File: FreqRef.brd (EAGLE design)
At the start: 50.8 x 43.2 mm, 33 parts, among them J1 ISP Connector, J2 BNC_RIGHT-ANGLE, SW1 PWR, U1 ATMEGA328, U2 MIC5205, U3 SN74LV164APW

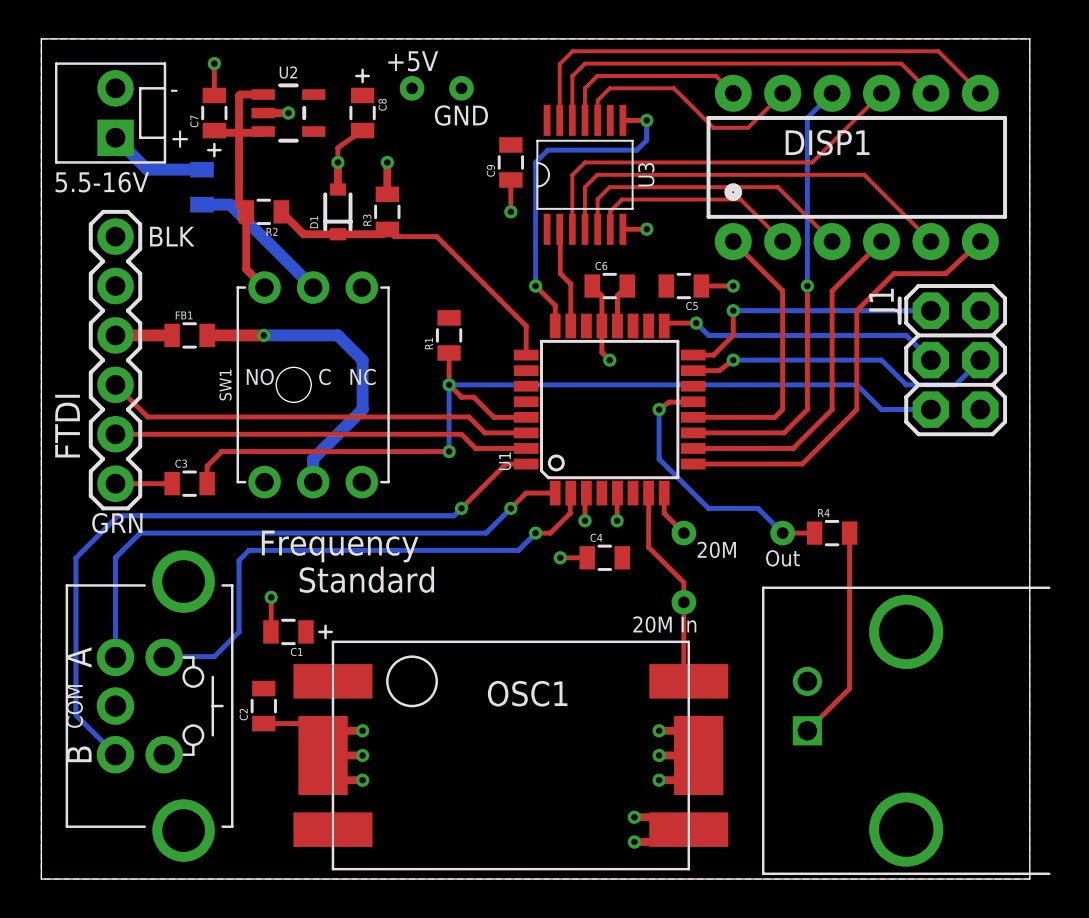
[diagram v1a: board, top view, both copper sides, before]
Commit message: More docs. Rev-B layout. Debugged sketch.
Continue documentation. Added two oscillator options to PCB schematic
and layout.  Debugged sketch  on Redboard.
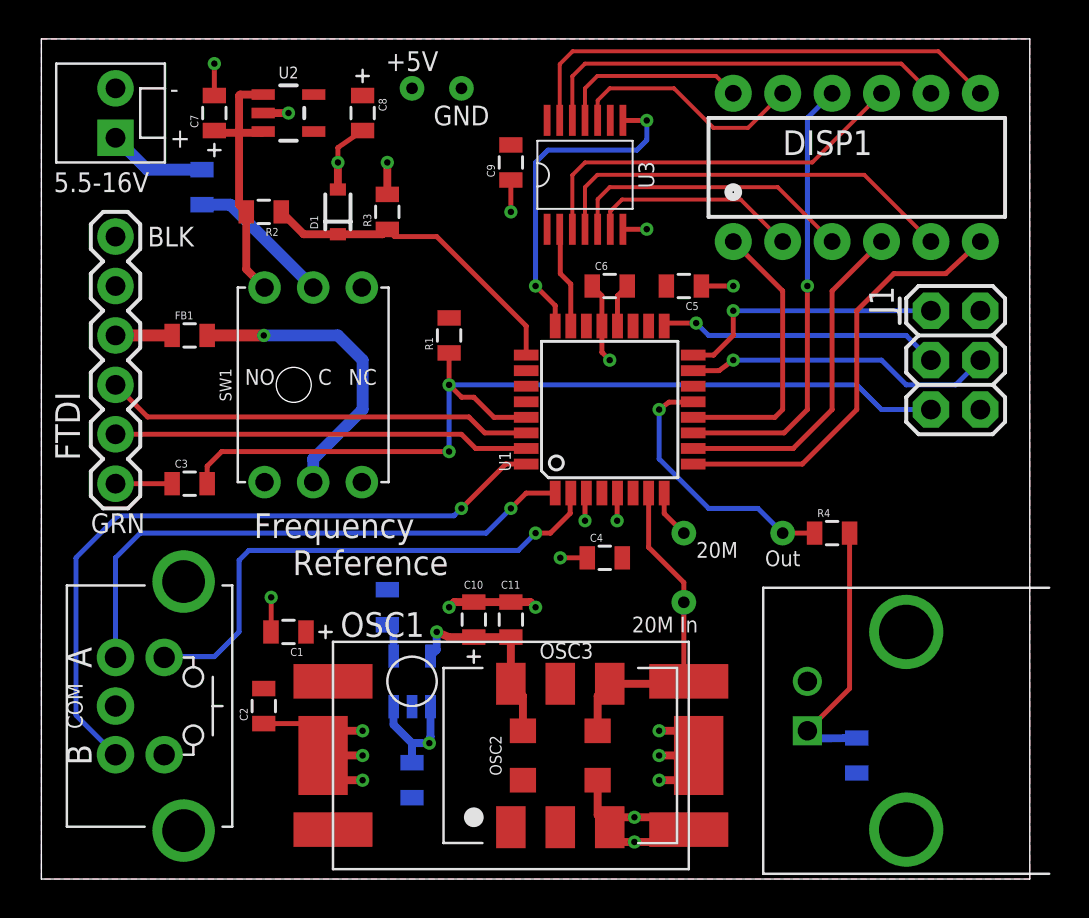
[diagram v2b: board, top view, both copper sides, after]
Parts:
- added C10, C13: 10uF, ChipsParts:0805-POL
- added C11: 10nF, SparkFun-Capacitors:0805
- added C12: 470pF, SparkFun-Capacitors:0805
- added C14: 50pF, SparkFun-Capacitors:0805
- added OSC2: (no value), playground:TCXO-3.2X5
- added OSC3: (no value), playground:TCXO-9X14
- added U5: MIC5219 3.3V, SparkFun-PowerIC:SOT23-5
- U1: value ATMEGA328 -> ATMEGA328P
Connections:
- net N$31 renamed VIN
- removed net N$5: OSC1.OUT, TP3.P$1, U1.7
- new net N$14: C10.1, C11.1, OSC2.8, OSC3.6, U5.5
- new net N$15: C12.1, U5.4
- new net OSCIN: OSC1.OUT, OSC2.5, OSC3.4, TP3.P$1, U1.7
- net GND: now also C10.2, C11.2, C12.2, C13.2, C14.2, OSC2.4, OSC3.3, U5.2
- net N$11: now also C14.1
- net VCC: now also C13.1, U5.1, U5.3
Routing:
- net OSCIN: track 0.00 -> 17.4 mm
- net GND: track 42.7 -> 53.7 mm, vias 20 -> 22
- net N$5: track 10.5 -> 0.00 mm
- net N$14: track 0.00 -> 10.3 mm, vias 0 -> 1
- net VCC: track 0.00 -> 6.04 mm, vias 0 -> 1
- net N$11: track 11.1 -> 13.7 mm
- net N$15: track 0.00 -> 1.74 mm
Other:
- board text added: "Frequency Reference"
- board text added: "http://github.com/uchip/FrequencyReference"
- board text removed: "Frequency Standard"
- board text removed: "http://github.com/uchip/FrequencyStandard"
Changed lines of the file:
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@@
 <text x="30.353" y="13.081" size="0.8128" layer="21" font="vector" ratio="15" align="center-left">20M In</text>
 <text x="33.655" y="16.51" size="0.8128" layer="21" font="vector" ratio="15">20M</text>
-<text x="11.176" y="14.732" size="1.27" layer="21" font="vector" ratio="15">Frequency
-    Standard</text>
-<text x="46.99" y="5.08" size="1.27" layer="22" font="vector" ratio="15" rot="MR45">http://github.com/uchip/FrequencyStandard</text>
+<text x="10.922" y="15.621" size="1.27" layer="21" font="vector" ratio="15">Frequency
+    Reference</text>
+<text x="48.26" y="3.81" size="1.27" layer="22" font="vector" ratio="15" rot="MR45">http://github.com/uchip/FrequencyReference</text>
 </plain>
 <attributes>
@@
 <elements>
 <element name="OSC1" library="playground" package="TCXO" value="" x="24.13" y="6.35" smashed="yes">
-<attribute name="NAME" x="22.86" y="8.89" size="1.27" layer="25" font="vector" ratio="15"/>
+<attribute name="NAME" x="15.367" y="12.446" size="1.27" layer="25" font="vector" ratio="15"/>
 <attribute name="VALUE" x="24.13" y="-1.27" size="1.27" layer="27" font="vector" ratio="15" align="bottom-center"/>
 </element>
@@
 <attribute name="VALUE" x="12.5095" y="40.3225" size="0.4064" layer="27" rot="R270"/>
 </element>
-<element name="U1" library="SparkFun" package="TQFP32-08" value="ATMEGA328" x="29.21" y="24.13" smashed="yes" rot="R90">
+<element name="U1" library="SparkFun" package="TQFP32-08" value="ATMEGA328P" x="29.21" y="24.13" smashed="yes" rot="R90">
 <attribute name="NAME" x="24.13" y="20.955" size="0.6096" layer="25" ratio="15" rot="R90"/>
 <attribute name="VALUE" x="35.56" y="21.59" size="0.4064" layer="27" rot="R90"/>
@@
 </element>
 <element name="FRAME1" library="NewFrame" package="FR-LTR-ON-PCB" value="FRAME_LTR_CU_MARK" x="49.53" y="17.78">
-<attribute name="CNAME" value="Frequency Standard" x="49.53" y="17.78" size="1.778" layer="27" display="off"/>
-<attribute name="CREVISION" value="Rev B" x="49.53" y="17.78" size="1.778" layer="27" display="off"/>
+<attribute name="CNAME" value="Frequency Reference" x="49.53" y="17.78" size="1.778" layer="27" display="off"/>
+<attribute name="CREVISION" value="Rev-B" x="49.53" y="17.78" size="1.778" layer="27" display="off"/>
 <attribute name="DATECODE" value="2015" x="49.53" y="17.78" size="1.778" layer="27" display="off"/>
 <attribute name="DESIGNER" value="C.Schnarel" x="49.53" y="17.78" size="1.778" layer="27" display="off"/>
 </element>
 <element name="TP4" library="ChipsParts" package="BBD-VIA" value="TEST_POINT" x="33.02" y="17.78"/>
+<element name="OSC2" library="playground" package="TCXO-3.2X5" value="" x="26.67" y="6.35" smashed="yes" rot="R270">
+<attribute name="NAME" x="23.654" y="6.35" size="0.6096" layer="25" font="vector" ratio="15" rot="R90" align="bottom-center"/>
+<attribute name="VALUE" x="26.67" y="4.35" size="0.6096" layer="25" font="vector" ratio="15" align="top-center"/>
+</element>
+<element name="OSC3" library="playground" package="TCXO-9X14" value="" x="26.67" y="6.35" smashed="yes" rot="R270">
+<attribute name="NAME" x="25.599" y="11.326" size="0.8128" layer="25" font="vector" ratio="15"/>
+<attribute name="VALUE" x="20.17" y="6.35" size="0.8128" layer="27" font="vector" ratio="15" rot="R270" align="top-center"/>
+</element>
+<element name="C10" library="ChipsParts" package="0805-POL" value="10uF" x="22.225" y="13.335" smashed="yes" rot="R90">
+<attribute name="NAME" x="21.717" y="14.9225" size="0.4064" layer="25" ratio="15"/>
+<attribute name="VALUE" x="23.622" y="12.319" size="0.4064" layer="27" rot="R90"/>
+</element>
+<element name="C11" library="SparkFun-Capacitors" package="0805" value="10nF" x="24.13" y="13.335" smashed="yes" rot="R90">
+<attribute name="NAME" x="23.622" y="14.9225" size="0.4064" layer="25" ratio="15"/>
+<attribute name="VALUE" x="25.527" y="12.319" size="0.4064" layer="27" rot="R90"/>
+</element>
+<element name="C12" library="SparkFun-Capacitors" package="0805" value="470pF" x="17.78" y="13.97" rot="MR90"/>
+<element name="C13" library="ChipsParts" package="0805-POL" value="10uF" x="19.05" y="5.08" rot="MR270"/>
+<element name="U5" library="SparkFun-PowerIC" package="SOT23-5" value="MIC5219 3.3V" x="19.05" y="10.16" rot="MR0">
+<attribute name="PROD_ID" value="VREG-09872" x="19.05" y="10.16" size="1.778" layer="28" rot="MR0" display="off"/>
+</element>
+<element name="C14" library="SparkFun-Capacitors" package="0805" value="50pF" x="41.91" y="6.35" smashed="yes" rot="MR270">
+<attribute name="NAME" x="41.0845" y="7.112" size="0.4064" layer="26" ratio="15" rot="MR270"/>
+<attribute name="VALUE" x="43.307" y="7.366" size="0.4064" layer="28" rot="MR270"/>
+</element>
 </elements>
 <signals>
@@
 <wire x1="31.75" y1="2.54" x2="31.75" y2="3.175" width="0.4064" layer="1"/>
 <wire x1="31.75" y1="2.54" x2="33.274" y2="2.54" width="0.4064" layer="1"/>
+<contactref element="C10" pad="2"/>
+<contactref element="OSC3" pad="3"/>
+<contactref element="OSC2" pad="4"/>
+<contactref element="C11" pad="2"/>
+<via x="25.4" y="13.97" extent="1-16" drill="0.3302"/>
+<via x="20.955" y="13.97" extent="1-16" drill="0.3302"/>
+<wire x1="24.13" y1="14.235" x2="25.135" y2="14.235" width="0.4064" layer="1"/>
+<wire x1="25.135" y1="14.235" x2="25.4" y2="13.97" width="0.4064" layer="1"/>
+<wire x1="24.13" y1="14.235" x2="22.225" y2="14.235" width="0.4064" layer="1"/>
+<wire x1="22.225" y1="14.235" x2="21.22" y2="14.235" width="0.4064" layer="1"/>
+<wire x1="21.22" y1="14.235" x2="20.955" y2="13.97" width="0.4064" layer="1"/>
+<wire x1="28.59" y1="5.08" x2="28.59" y2="3.285" width="0.4064" layer="1"/>
+<wire x1="28.59" y1="3.285" x2="29.21" y2="2.665" width="0.4064" layer="1"/>
+<contactref element="C13" pad="2"/>
+<contactref element="C12" pad="2"/>
+<contactref element="U5" pad="2"/>
+<contactref element="C14" pad="2"/>
+<wire x1="30.48" y1="1.905" x2="29.21" y2="1.905" width="0.4064" layer="1"/>
+<wire x1="29.21" y1="1.905" x2="29.21" y2="2.54" width="0.4064" layer="1"/>
+<wire x1="30.48" y1="3.175" x2="29.21" y2="3.175" width="0.4064" layer="1"/>
+<wire x1="29.21" y1="3.175" x2="29.21" y2="2.665" width="0.4064" layer="1"/>
 <wire x1="33.02" y1="6.35" x2="33.782" y2="6.35" width="0" layer="19" extent="1-1"/>
 </signal>
@@
 <contactref element="U3" pad="9"/>
 <contactref element="U3" pad="1"/>
+<contactref element="U5" pad="3"/>
+<contactref element="C13" pad="1"/>
+<contactref element="U5" pad="1"/>
+<wire x1="20" y1="8.8599" x2="20" y2="7.305" width="0.4064" layer="16"/>
+<wire x1="20" y1="7.305" x2="19.939" y2="6.985" width="0.4064" layer="16"/>
+<via x="19.939" y="6.985" extent="1-16" drill="0.3302"/>
+<wire x1="19.05" y1="6.985" x2="18.1" y2="7.935" width="0.4064" layer="16"/>
+<wire x1="18.1" y1="7.935" x2="18.1" y2="8.8599" width="0.4064" layer="16"/>
+<wire x1="19.05" y1="6.985" x2="19.939" y2="6.985" width="0.4064" layer="16"/>
+<wire x1="19.05" y1="5.98" x2="19.05" y2="6.985" width="0.4064" layer="16"/>
 </signal>
 <signal name="RAW" class="1">
@@
 <wire x1="38.1" y1="17.78" x2="39.74" y2="17.78" width="0.254" layer="1"/>
 </signal>
-<signal name="N$5">
+<signal name="OSCIN">
 <contactref element="U1" pad="7"/>
 <contactref element="OSC1" pad="OUT"/>
@@
 <wire x1="33.02" y1="10.414" x2="33.274" y2="10.16" width="0.254" layer="1"/>
 <contactref element="TP3" pad="P$1"/>
+<contactref element="OSC2" pad="5"/>
+<contactref element="OSC3" pad="4"/>
+<wire x1="29.21" y1="10.035" x2="33.274" y2="10.035" width="0.4064" layer="1"/>
+<wire x1="33.274" y1="10.035" x2="33.274" y2="10.16" width="0.4064" layer="1"/>
+<wire x1="28.59" y1="7.62" x2="28.59" y2="9.415" width="0.4064" layer="1"/>
+<wire x1="28.59" y1="9.415" x2="29.21" y2="10.035" width="0.4064" layer="1"/>
 <wire x1="33.02" y1="15.24" x2="33.02" y2="14.224" width="0" layer="19" extent="1-1"/>
 </signal>
@@
 <wire x1="3.81" y1="27.94" x2="6.72" y2="27.94" width="0.6096" layer="1"/>
 </signal>
-<signal name="N$31">
+<signal name="VIN">
 <contactref element="SW1" pad="2C"/>
 <wire x1="9.71" y1="34.66" x2="13.97" y2="30.4" width="0.6096" layer="16"/>
@@
 <wire x1="39.37" y1="7.62" x2="41.54" y2="9.79" width="0.254" layer="1"/>
 <wire x1="41.54" y1="9.79" x2="41.54" y2="17.78" width="0.254" layer="1"/>
+<contactref element="C14" pad="1"/>
+<wire x1="41.91" y1="7.25" x2="39.867" y2="7.228" width="0.4064" layer="16"/>
+<wire x1="39.867" y1="7.228" x2="39.37" y2="7.62" width="0.4064" layer="16"/>
 </signal>
 <signal name="N$13">
@@
 <wire x1="5.45" y1="36.46" x2="8.255" y2="36.46" width="0.6096" layer="16"/>
 </signal>
+<signal name="N$14">
+<contactref element="OSC3" pad="6"/>
+<contactref element="C10" pad="1"/>
+<contactref element="C11" pad="1"/>
+<contactref element="OSC2" pad="8"/>
+<wire x1="24.13" y1="12.435" x2="24.13" y2="10.035" width="0.4064" layer="1"/>
+<wire x1="24.75" y1="7.62" x2="24.75" y2="9.415" width="0.4064" layer="1"/>
+<wire x1="24.75" y1="9.415" x2="24.13" y2="10.035" width="0.4064" layer="1"/>
+<wire x1="20.944" y1="12.435" x2="20.32" y2="12.7" width="0.4064" layer="1"/>
+<via x="20.32" y="12.7" extent="1-16" drill="0.3302"/>
+<contactref element="U5" pad="5"/>
+<wire x1="20.32" y1="12.7" x2="20.32" y2="11.7801" width="0.4064" layer="16"/>
+<wire x1="20.32" y1="11.7801" x2="20" y2="11.4601" width="0.4064" layer="16"/>
+<wire x1="20.944" y1="12.435" x2="22.225" y2="12.435" width="0.4064" layer="1"/>
+<wire x1="22.225" y1="12.435" x2="24.13" y2="12.435" width="0.4064" layer="1"/>
+</signal>
+<signal name="N$15">
+<contactref element="C12" pad="1"/>
+<contactref element="U5" pad="4"/>
+<wire x1="18.1" y1="11.4601" x2="18.1" y2="12.75" width="0.4064" layer="16"/>
+<wire x1="18.1" y1="12.75" x2="17.78" y2="13.07" width="0.4064" layer="16"/>
+</signal>
 </signals>

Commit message: Software debug.  Schematic values. Added photos.
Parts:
- R2: value 15k -> 10k
- R3: value 5k -> 3.3k
- moved C3 12.8 mm to (6.35, 33.0)
- moved FTDI 12.8 mm to (2.54, 33.0), turned to 270 degrees
- moved FB1 5.08 mm to (7.62, 22.9)
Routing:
- net N$32: track 15.8 -> 7.17 mm
- net TXO: track 21.4 -> 29.3 mm
- net VCCUSB: track 2.91 -> 4.89 mm
- net RXI: track 22.1 -> 23.6 mm
- net RESET: track 48.7 -> 50.0 mm
